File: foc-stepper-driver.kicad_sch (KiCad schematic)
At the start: 0 parts

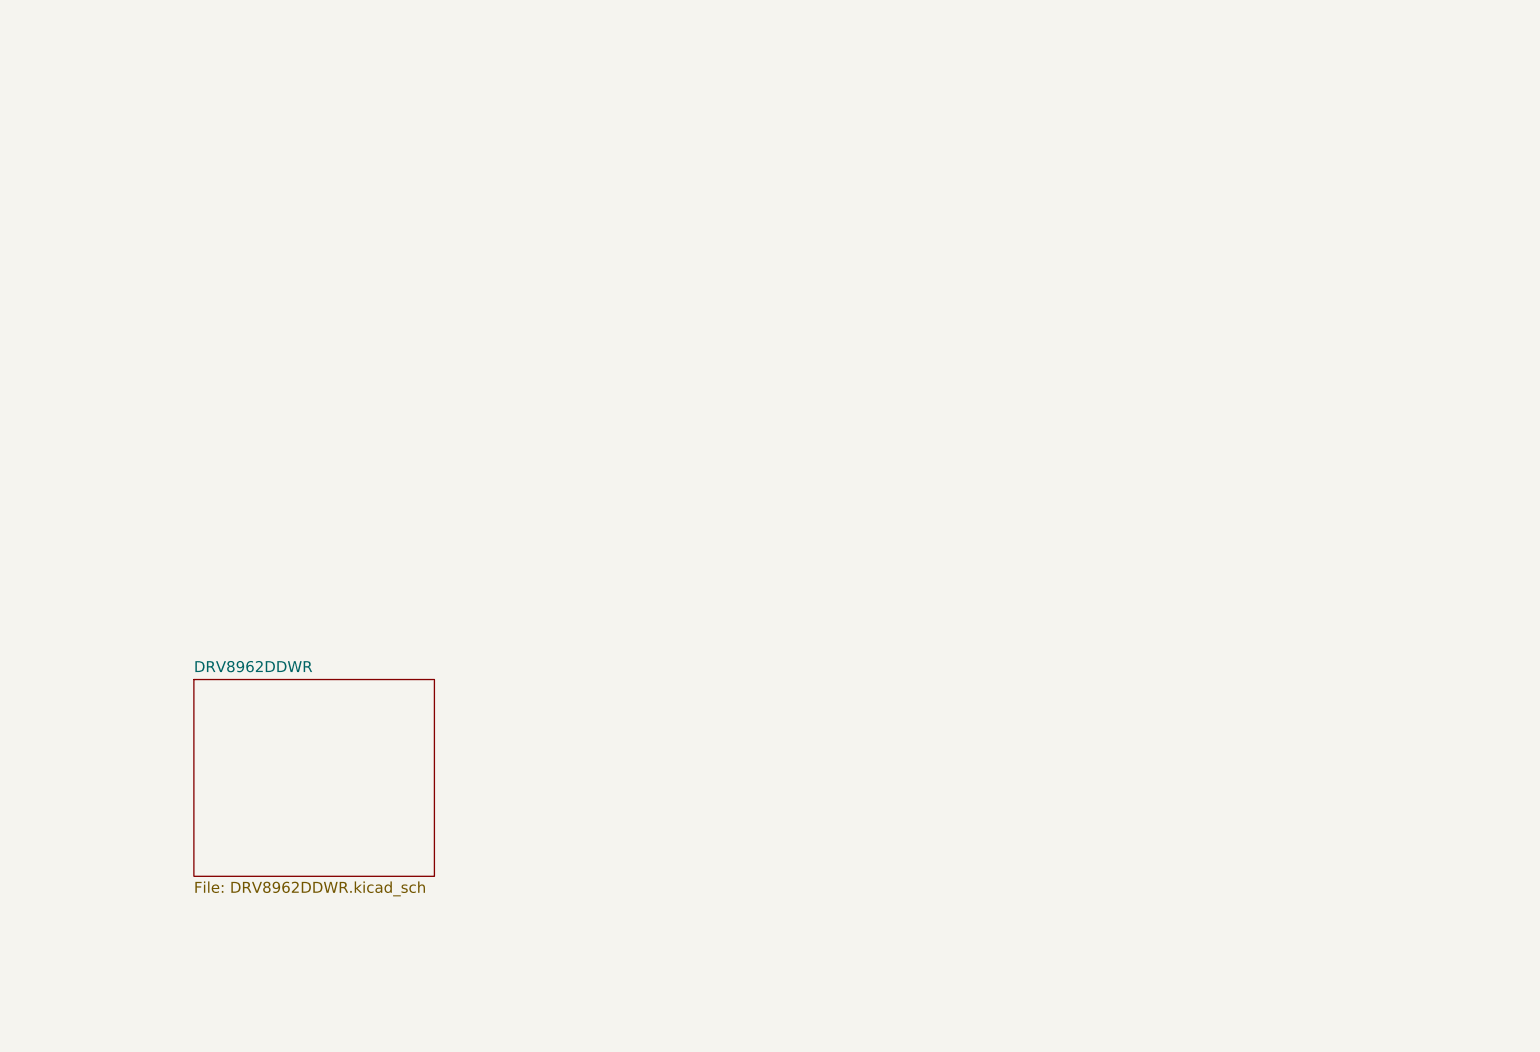
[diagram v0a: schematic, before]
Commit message: feat: add as5047p
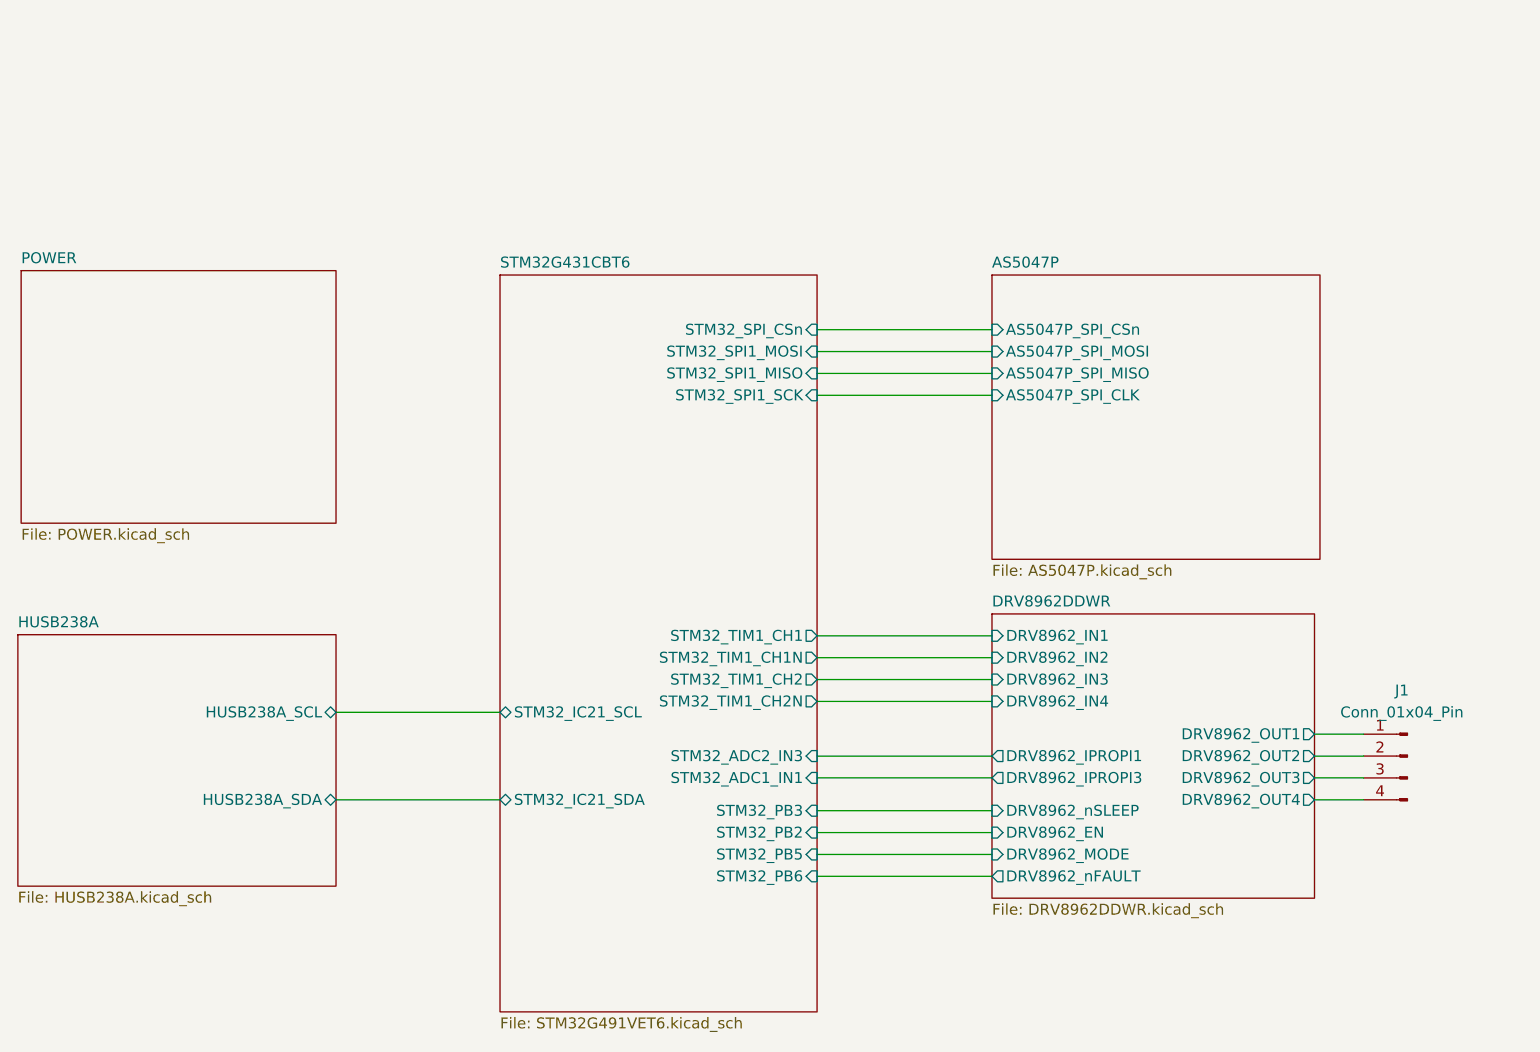
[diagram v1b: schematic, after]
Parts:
- added J1: Conn_01x04_Pin, symbol Connector:Conn_01x04_Pin
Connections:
- new net DRV8962DDWR/DRV8962_OUT1: J1.1 (Pin_1)
- new net DRV8962DDWR/DRV8962_OUT2: J1.2 (Pin_2)
- new net DRV8962DDWR/DRV8962_OUT3: J1.3 (Pin_3)
- new net DRV8962DDWR/DRV8962_OUT4: J1.4 (Pin_4)
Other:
- added sheet AS5047P (AS5047P.kicad_sch)
- added sheet HUSB238A (HUSB238A.kicad_sch)
- added sheet POWER (POWER.kicad_sch)
- added sheet STM32G431CBT6 (STM32G491VET6.kicad_sch)
- sheet DRV8962DDWR ports: added DRV8962_EN, DRV8962_IN1, DRV8962_IN2, DRV8962_IN3, DRV8962_IN4, DRV8962_IPROPI1, DRV8962_IPROPI3, DRV8962_MODE, DRV8962_OUT1, DRV8962_OUT2, DRV8962_OUT3, DRV8962_OUT4, DRV8962_nFAULT, DRV8962_nSLEEP; removed none

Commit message: feat: add can and usart connector
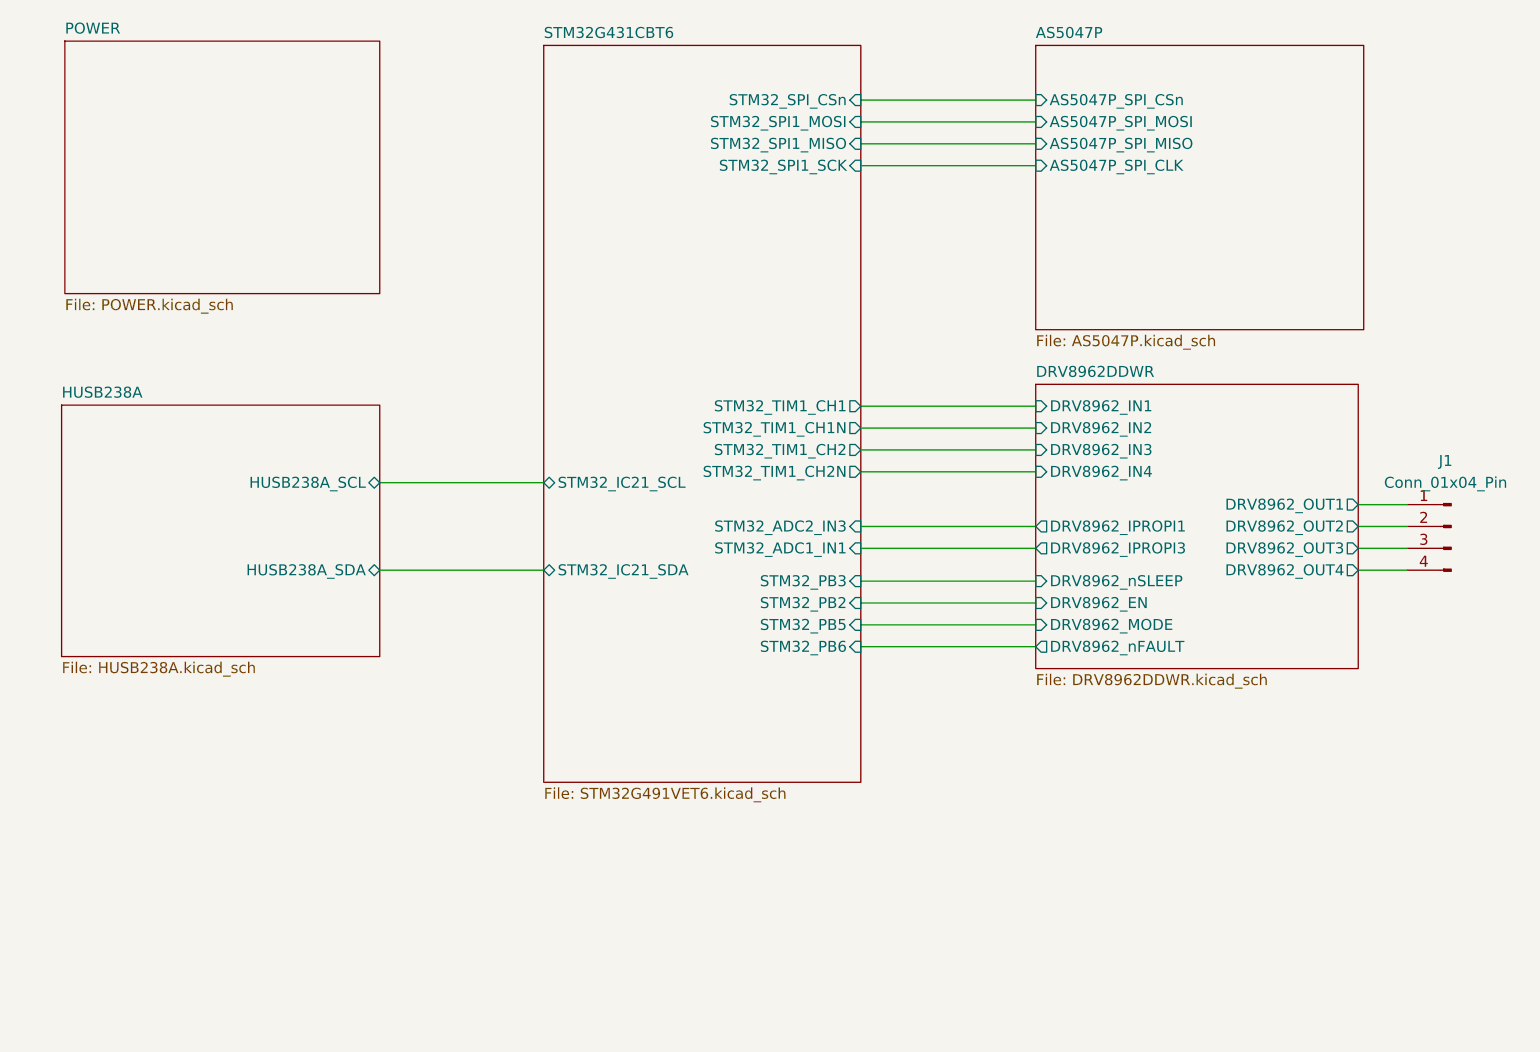
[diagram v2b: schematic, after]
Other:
- moved on the sheet: J1

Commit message: change components
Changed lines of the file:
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@@
 		(size 36.957 29.21)
 		(exclude_from_sim no)
-		(in_bom yes)
-		(on_board yes)
-		(dnp no)
+		(in_bom no)
+		(on_board no)
+		(dnp yes)
 		(fields_autoplaced yes)
 		(stroke
@@
 			)
 		)
-		(pin "AS5047P_SPI_MOSI" input
+		(pin "AS5047P_SPI_MOSI" tri_state
 			(at 181.61 58.42 180)
 			(effects
@@
 			)
 		)
-		(pin "AS5047P_SPI_MISO" input
+		(pin "AS5047P_SPI_MISO" tri_state
 			(at 181.61 60.96 180)
 			(effects
@@
 			)
 		)
-		(pin "AS5047P_SPI_CLK" input
+		(pin "AS5047P_SPI_CLK" tri_state
 			(at 181.61 63.5 180)
 			(effects
@@
 			)
 		)
-		(pin "AS5047P_SPI_CSn" input
+		(pin "AS5047P_SPI_CSn" tri_state
 			(at 181.61 55.88 180)
 			(effects
@@
 			)
 		)
-		(pin "STM32_SPI1_MOSI" input
+		(pin "STM32_SPI1_MOSI" tri_state
 			(at 161.29 58.42 0)
 			(effects
@@
 			)
 		)
-		(pin "STM32_SPI1_MISO" input
+		(pin "STM32_SPI1_MISO" tri_state
 			(at 161.29 60.96 0)
 			(effects
@@
 			)
 		)
-		(pin "STM32_SPI1_SCK" input
+		(pin "STM32_SPI1_SCK" tri_state
 			(at 161.29 63.5 0)
 			(effects
@@
 			)
 		)
-		(pin "STM32_PB3" input
+		(pin "STM32_PB3" output
 			(at 161.29 111.76 0)
 			(effects
@@
 			)
 		)
-		(pin "STM32_PB2" input
+		(pin "STM32_PB2" output
 			(at 161.29 114.3 0)
 			(effects
@@
 			)
 		)
-		(pin "STM32_PB5" input
+		(pin "STM32_PB5" output
 			(at 161.29 116.84 0)
 			(effects
@@
 			)
 		)
-		(pin "STM32_SPI_CSn" input
+		(pin "STM32_SPI_CSn" tri_state
 			(at 161.29 55.88 0)
 			(effects

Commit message: update sch
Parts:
- J1: footprint (none) -> TerminalBlock:TerminalBlock_Xinya_XY308-2.54-4P_1x04_P2.54mm_Horizontal
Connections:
- no-connect marks 0 -> 2
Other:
- removed sheet HUSB238A
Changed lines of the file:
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@@
 	(generator_version "9.0")
 	(paper "A4")
-	(wire
-		(pts
-			(xy 219.075 110.49) (xy 224.79 110.49)
-		)
-		(stroke
-			(width 0)
-			(type default)
-		)
-	)
-	(wire
-		(pts
-			(xy 219.075 102.87) (xy 224.79 102.87)
+	(no_connect
+		(at 124.46 110.49)
+	)
+	(no_connect
+		(at 124.46 100.33)
+	)
+	(wire
+		(pts
+			(xy 218.44 110.49) (xy 224.79 110.49)
+		)
+		(stroke
+			(width 0)
+			(type default)
+		)
+	)
+	(wire
+		(pts
+			(xy 218.44 102.87) (xy 224.79 102.87)
 		)
 		(stroke
@@
 	(wire
 		(pts
-			(xy 219.075 105.41) (xy 224.79 105.41)
-		)
-		(stroke
-			(width 0)
-			(type default)
-		)
-	)
-	(wire
-		(pts
-			(xy 219.075 107.95) (xy 224.79 107.95)
+			(xy 218.44 105.41) (xy 224.79 105.41)
+		)
+		(stroke
+			(width 0)
+			(type default)
+		)
+	)
+	(wire
+		(pts
+			(xy 218.44 107.95) (xy 224.79 107.95)
 		)
 		(stroke
@@
 	(wire
 		(pts
-			(xy 105.41 110.49) (xy 124.46 110.49)
-		)
-		(stroke
-			(width 0)
-			(type default)
-		)
-	)
-	(wire
-		(pts
 			(xy 161.29 91.44) (xy 181.61 91.44)
 		)
@@
 		(pts
 			(xy 161.29 111.76) (xy 181.61 111.76)
-		)
-		(stroke
-			(width 0)
-			(type default)
-		)
-	)
-	(wire
-		(pts
-			(xy 105.41 100.33) (xy 124.46 100.33)
 		)
 		(stroke
@@
 			)
 		)
-		(property "Footprint" ""
+		(property "Footprint" "TerminalBlock:TerminalBlock_Xinya_XY308-2.54-4P_1x04_P2.54mm_Horizontal"
 			(at 229.87 105.41 0)
 			(effects
@@
 	)
 	(sheet
-		(at 68.453 91.313)
-		(size 36.957 29.21)
-		(exclude_from_sim no)
-		(in_bom no)
-		(on_board no)
-		(dnp yes)
-		(fields_autoplaced yes)
-		(stroke
-			(width 0.1524)
-			(type solid)
-		)
-		(fill
-			(color 255 255 194 1.0000)
-		)
-		(property "Sheetname" "HUSB238A"
-			(at 68.453 90.6014 0)
-			(effects
-				(font
-					(size 1.27 1.27)
-				)
-				(justify left bottom)
-			)
-		)
-		(property "Sheetfile" "HUSB238A.kicad_sch"
-			(at 68.453 121.1076 0)
-			(effects
-				(font
-					(size 1.27 1.27)
-				)
-				(justify left top)
-			)
-		)
-		(pin "HUSB238A_SDA" bidirectional
-			(at 105.41 110.49 0)
-			(effects
-				(font
-					(size 1.27 1.27)
-				)
-				(justify right)
-			)
-		)
-		(pin "HUSB238A_SCL" bidirectional
-			(at 105.41 100.33 0)
-			(effects
-				(font
-					(size 1.27 1.27)
-				)
-				(justify right)
-			)
-		)
-		(instances
-			(project "foc-stepper-driver"
-				(path "/e8a1091a-f86c-4a0e-9f89-1944d2e62a64"
-					(page "4")
-				)
-			)
-		)
-	)
-	(sheet
 		(at 181.61 49.53)
 		(size 38.1 33.02)
@@
 	(sheet
 		(at 181.61 88.9)
-		(size 37.465 33.02)
+		(size 36.83 33.02)
 		(exclude_from_sim no)
 		(in_bom yes)
@@
 		)
 		(pin "DRV8962_OUT1" output
-			(at 219.075 102.87 0)
+			(at 218.44 102.87 0)
 			(effects
 				(font
@@
 		)
 		(pin "DRV8962_OUT2" output
-			(at 219.075 105.41 0)
+			(at 218.44 105.41 0)
 			(effects
 				(font
@@
 		)
 		(pin "DRV8962_OUT3" output
-			(at 219.075 107.95 0)
+			(at 218.44 107.95 0)
 			(effects
 				(font
@@
 		)
 		(pin "DRV8962_OUT4" output
-			(at 219.075 110.49 0)
-			(effects
-				(font
+			(at 218.44 110.49 0)
+			(effects
+				(font
